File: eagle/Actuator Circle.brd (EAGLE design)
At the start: 50.2 x 46.3 mm, 28 parts, among them Q1 FDV301N

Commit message: Modified Resistors to 0603, and moved them to the same side
Modified Resistors to 0603, and moved them to the same side, so as to make assembly slightly easier.
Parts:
- R2, R3, R4, R5, R6: device Actuator Circle:RES_0402 -> resistor:R0603
- moved R2 13.3 mm to (6.10, 39.4), flipped to the top, turned to 90 degrees
- moved LED2 4.33 mm to (36.8, 45.0), flipped to the top, turned to 270 degrees
- moved R5 1.37 mm to (33.7, 44.4), flipped to the top, turned to 270 degrees
- moved R3 0.72 mm to (10.2, 44.7), turned to 220 degrees
- moved R6 0.57 mm to (40.9, 9.40), flipped to the top, turned to 225 degrees
- moved 5V 0.25 mm to (42.2, 8.13), flipped to the top, turned to 135 degrees
- moved R4 0.25 mm to (8.89, 42.4)
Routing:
- net NC: track 0.00 -> 17.1 mm, vias 0 -> 1
- net N$1: track 1.28 -> 17.9 mm, vias 0 -> 1
- net GND: track 183.2 -> 193.7 mm
- net FAN-IO25: track 59.0 -> 64.5 mm
- net STEP-IO4: track 36.6 -> 38.6 mm, vias 2 -> 1
- net 20V: track 64.7 -> 65.6 mm
- net FAN-GATE: track 8.23 -> 7.29 mm
- net N$2: track 1.61 -> 2.16 mm
- net 5V: vias 5 -> 6

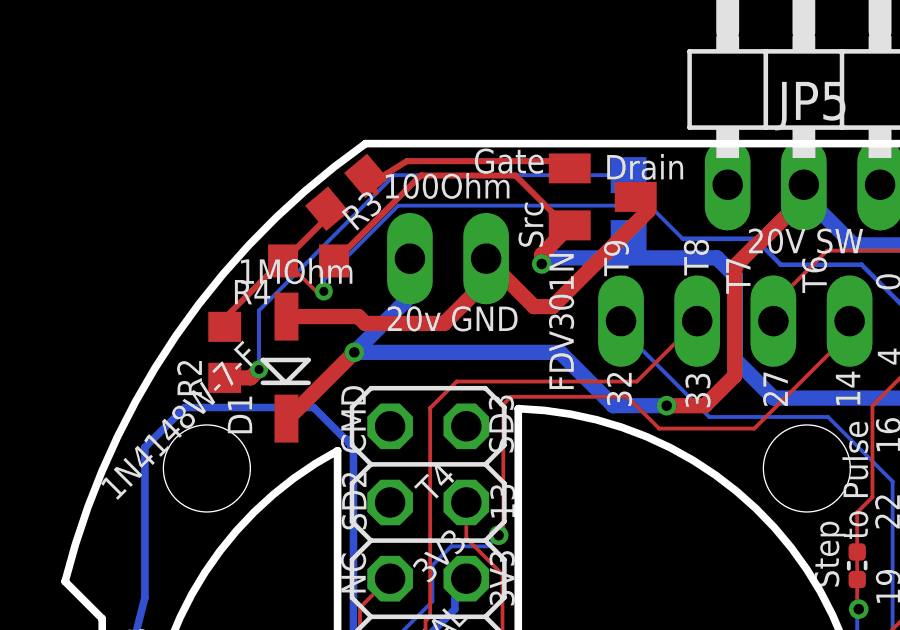
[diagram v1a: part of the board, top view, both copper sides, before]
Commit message: Update Actuator Circle.brd
Moved the vias further away from the top side resistors. Also covered vias with solder mask to minimise risk of shorts whilst soldering
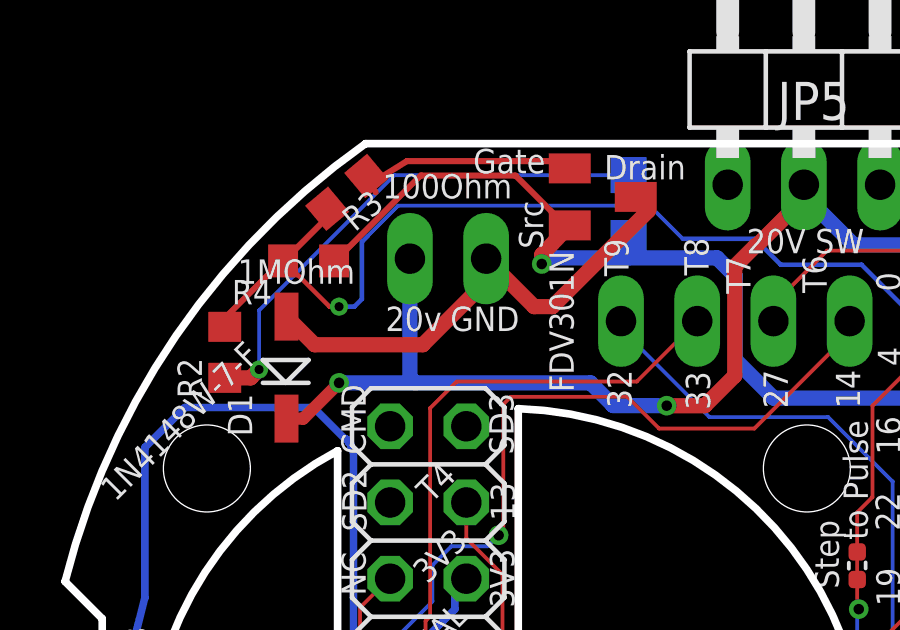
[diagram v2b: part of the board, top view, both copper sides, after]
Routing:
- net FAN-IO25: track 64.5 -> 66.1 mm
- net 20V-SW: track 108.9 -> 109.7 mm
- net DRAIN: track 16.1 -> 16.7 mm
